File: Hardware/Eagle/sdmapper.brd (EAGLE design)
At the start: 101 x 64.6 mm, 30 parts, among them IC1 AM29F010J, IC2 HM628512ASOP32, IC3 XC95144XL_TQ100, IC4 LM1117-3V3, T1 BC857, T2 BC857

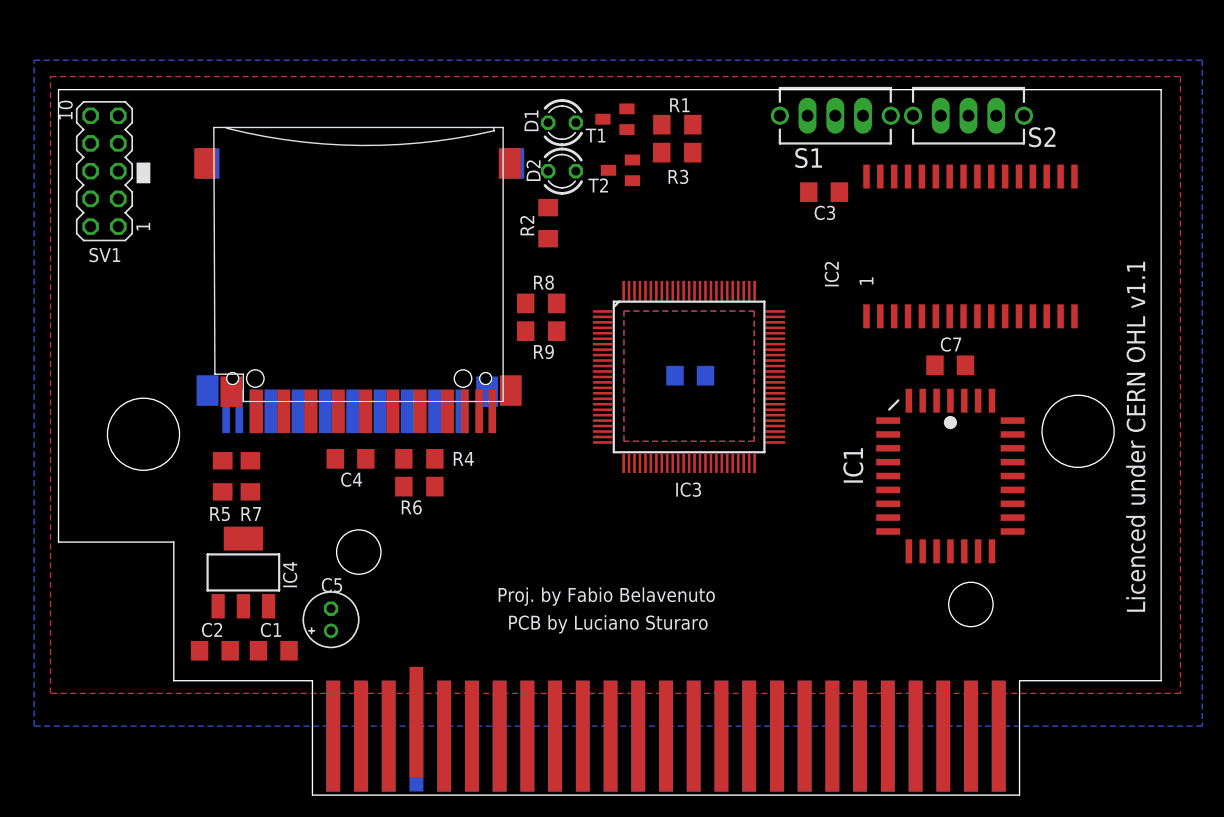
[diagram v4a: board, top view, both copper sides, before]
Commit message: CPLD com pinout do produto final. Adicionado versao 2.0.3 do Nextor. Mudado nome da ROM de NEXTOR.ROM para SDMAPPER.ROM Adicionado na inicializacao do driver a chamada a funcao INITXT para exibir mensagens em screen0. Adicionado utilitarios novos.
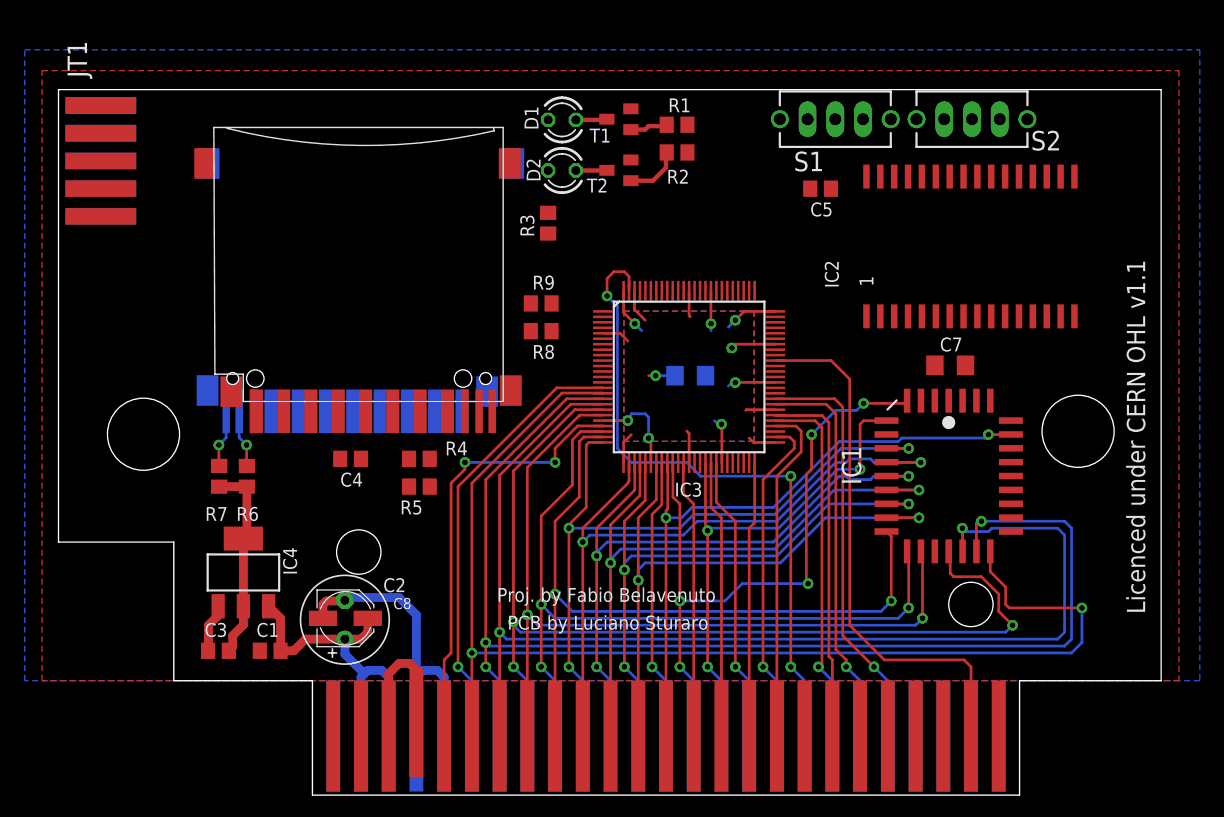
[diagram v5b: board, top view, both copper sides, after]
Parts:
- removed SV1: JTAG, con-lstb:MA05-2
- added C8: 100u, rcl:PANASONIC_C
- added JT1: (no value), JTAGs:SMD5X2
- C1, C3, C4: device rcl:C1206 -> rcl:C0805
- C2: value 100n -> 220u; device rcl:C1206 -> rcl:E3,5-8
- C5: value 220u -> 100n; device rcl:E2-5 -> rcl:C0805
- R1, R4, R5, R6, R7, R8, R9: device rcl:R1206 -> rcl:R0805
- R2: value 330 -> 4K7; device rcl:R1206 -> rcl:R0805
- R3: value 4K7 -> 330; device rcl:R1206 -> rcl:R0805
- T1, T2: value BC857 -> BC858
- moved C3 69.6 mm to (14.9, 12.9)
- moved C5 59.7 mm to (70.0, 55.2), turned to 0 degrees
- moved R5 18.0 mm to (33.3, 27.9), turned to 180 degrees
- moved R6 15.8 mm to (17.5, 28.9), turned to 270 degrees
- moved R3 13.5 mm to (45.1, 52.1), turned to 90 degrees
- moved R2 13.5 mm to (56.9, 58.5), turned to 0 degrees
- moved C2 12.2 mm to (26.5, 15.7), turned to 90 degrees
- moved R7 2.86 mm to (15.0, 28.9)
- moved R8 2.54 mm to (44.5, 42.2)
- moved R9 2.54 mm to (44.5, 44.7)
- moved S2 0.45 mm to (83.9, 61.6)
- moved T1 0.36 mm to (51.6, 61.6)
- moved C1 0.32 mm to (19.6, 12.9)
- moved S1 0.32 mm to (71.4, 61.6)
- moved D1 0.25 mm to (46.4, 61.5)
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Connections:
- removed net MR_MP: IC3.1, R8.1, S2.2
- new net SEL_MR_MP: IC3.1, R9.1, S2.2
- net +3V3: now also C3.2; no longer C2.2
- net DIS_MR_MP: now also R8.1; no longer R9.1
- net GND: now also C2.-, C5.1, C8.-, JT1.GND@1, JT1.GND@2, R3.1; no longer C2.1, C5.-, IC1.1, R2.1, SV1.10, SV1.2
- net N$5: now also R2.1; no longer R3.1
- net N$7: now also R3.2; no longer R2.2
- net SD_CD1: now also R6.1; no longer R7.1
- net SD_CS1: now also R2.2; no longer R3.2
- net SD_WP0: now also R5.1; no longer R6.1
- net SD_WP1: now also R7.1; no longer R5.1
- net TCK: now also JT1.TCK; no longer SV1.1
- net TDI: now also JT1.TDI; no longer SV1.9
- net TDO: now also JT1.TDO; no longer SV1.3
- net TMS: now also JT1.TMS; no longer SV1.5
- net VCC: now also C2.+, C5.2, C8.+, JT1.+3V3; no longer C3.2, C5.+, SV1.4
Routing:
- net CPU_D5: track 0.00 -> 113.7 mm, vias 0 -> 3
- net CPU_D6: track 0.00 -> 110.6 mm, vias 0 -> 2
- net CPU_D4: track 0.00 -> 109.2 mm, vias 0 -> 2
- net CPU_D3: track 0.00 -> 92.6 mm, vias 0 -> 3
- net CPU_D2: track 0.00 -> 76.6 mm, vias 0 -> 2
- net CPU_D1: track 0.00 -> 71.8 mm, vias 0 -> 3
- net GND: track 0.00 -> 70.1 mm, vias 0 -> 8
- net CPU_D0: track 0.00 -> 68.6 mm, vias 0 -> 2
- net CPU_A5: track 0.00 -> 66.2 mm, vias 0 -> 3
- net CPU_A4: track 0.00 -> 64.1 mm, vias 0 -> 2
- net CPU_A12: track 0.00 -> 62.2 mm, vias 0 -> 5
- net CPU_A3: track 0.00 -> 61.1 mm, vias 0 -> 3
- net RESET: track 0.00 -> 61.0 mm, vias 0 -> 3
- net CPU_A2: track 0.00 -> 60.3 mm, vias 0 -> 2
- net CPU_A13: track 0.00 -> 59.8 mm, vias 0 -> 2
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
